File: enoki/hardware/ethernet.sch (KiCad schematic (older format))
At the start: 2 parts

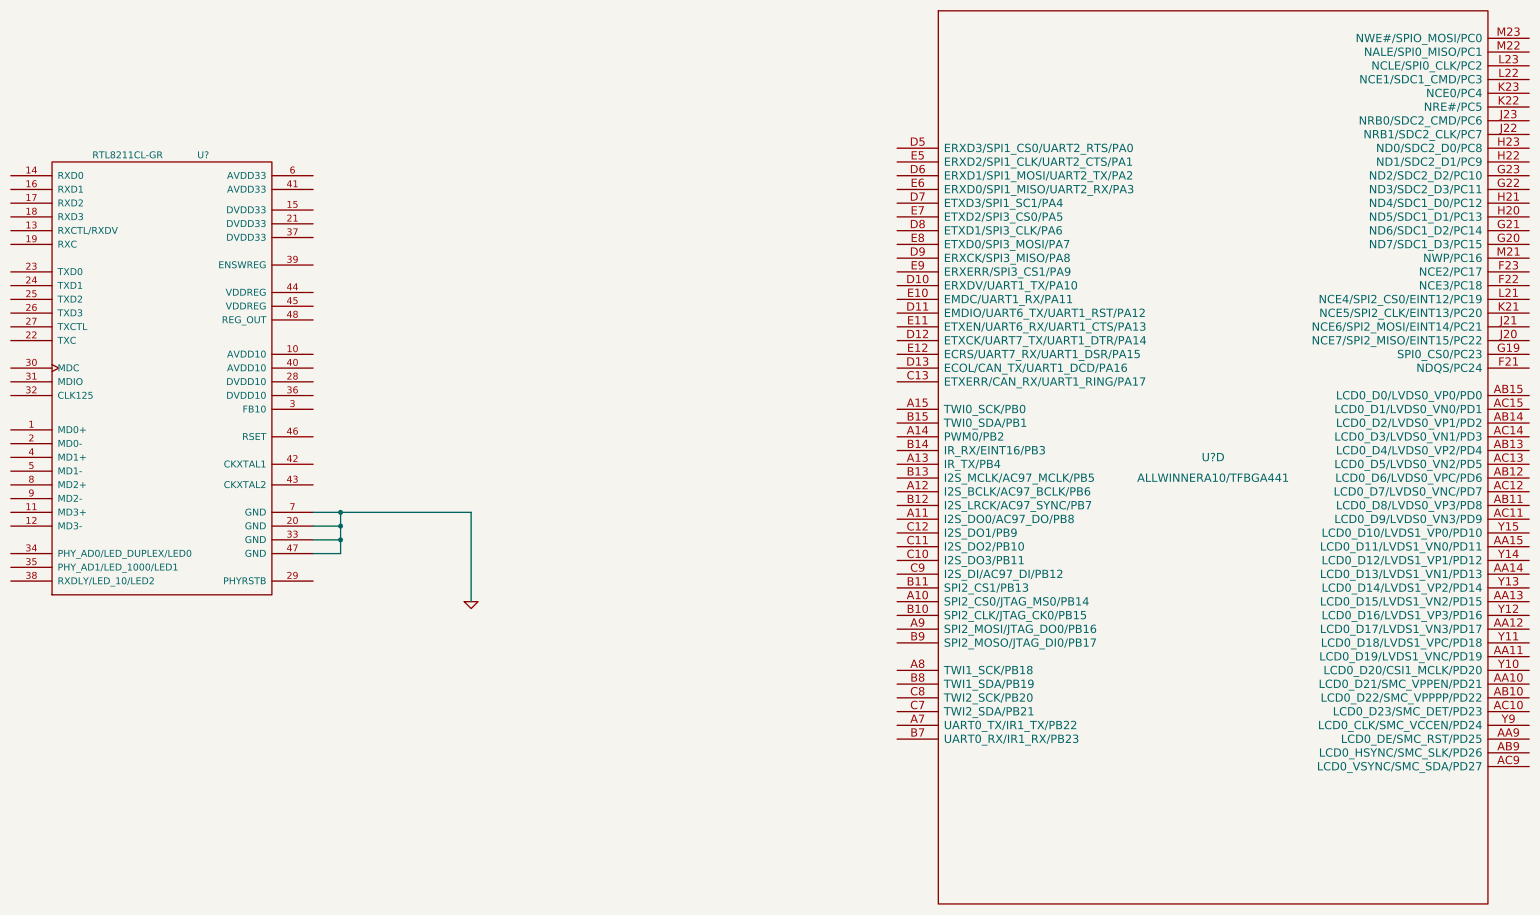
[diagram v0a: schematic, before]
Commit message: ethernet lib added
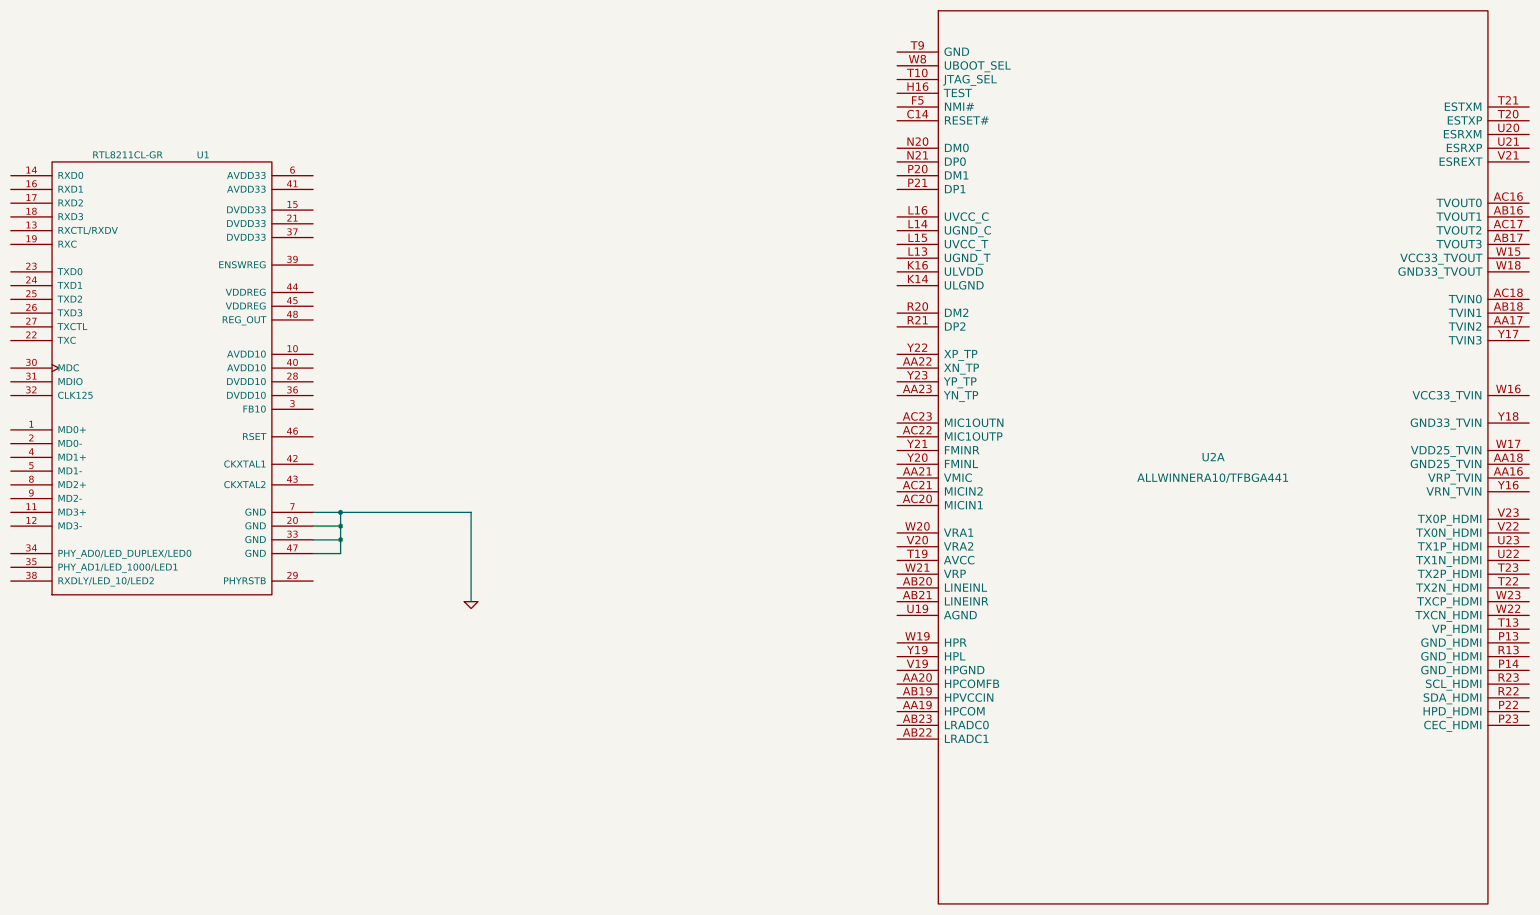
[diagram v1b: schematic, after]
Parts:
- gave numbers to parts that had none: 2
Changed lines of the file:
@@
 LIBS:allwinner
 LIBS:RTL8211CL-GR
+LIBS:enoki-cache
 EELAYER 27 0
 EELAYER END
 $Descr A1 33110 23386
 encoding utf-8
-Sheet 1 1
+Sheet 2 2
 Title ""
 Date "9 mar 2015"
@@
 $EndDescr
 $Comp
-L ALLWINNERA10/TFBGA441 U?
-U 4 1 54FDA219
+L ALLWINNERA10/TFBGA441 U2
+U 1 1 54FDA219
 P 11400 7400
-F 0 "U?" H 11400 7400 60  0000 C CNN
+F 0 "U2" H 11400 7400 60  0000 C CNN
 F 1 "ALLWINNERA10/TFBGA441" H 11400 7250 60  0000 C CNN
 F 2 "" H 11400 7400 60  0000 C CNN
 F 3 "" H 11400 7400 60  0000 C CNN
-	4    11400 7400
+	1    11400 7400
 	1    0    0    -1
 $EndComp
 $Comp
-L RTL8211CL-GR U?
+L RTL8211CL-GR U1
 U 1 1 54FDAE8D
 P 3700 6600
-F 0 "U?" H 4050 8000 50  0000 C CNN
+F 0 "U1" H 4050 8000 50  0000 C CNN
 F 1 "RTL8211CL-GR" H 3500 8000 50  0000 C CNN
 F 2 "MODULE" H 3700 6600 50  0001 C CNN
@@
 $EndComp
 $Comp
-L GND #PWR?
+L GND #PWR1
 U 1 1 54FDD4EF
 P 6000 8450
-F 0 "#PWR?" H 6000 8450 30  0001 C CNN
+F 0 "#PWR1" H 6000 8450 30  0001 C CNN
 F 1 "GND" H 6000 8380 30  0001 C CNN
 F 2 "" H 6000 8450 60  0000 C CNN
